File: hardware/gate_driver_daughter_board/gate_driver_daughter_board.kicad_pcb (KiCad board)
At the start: 2 copper layers, 103 x 116.3 mm, 66 parts, among them J1 Conn_01x08, J2 Conn_01x02, J3 Conn_01x02, U1 LF33_TO220, U2 REC20K-2412SZ, U3 6N137, U4 NCD57100DWR2G, U5 LTC6992CS6-2-TRMPBF, U6 LM7805_TO220, U7 MCP6004, U8 INA826, U9 LM7805_TO220

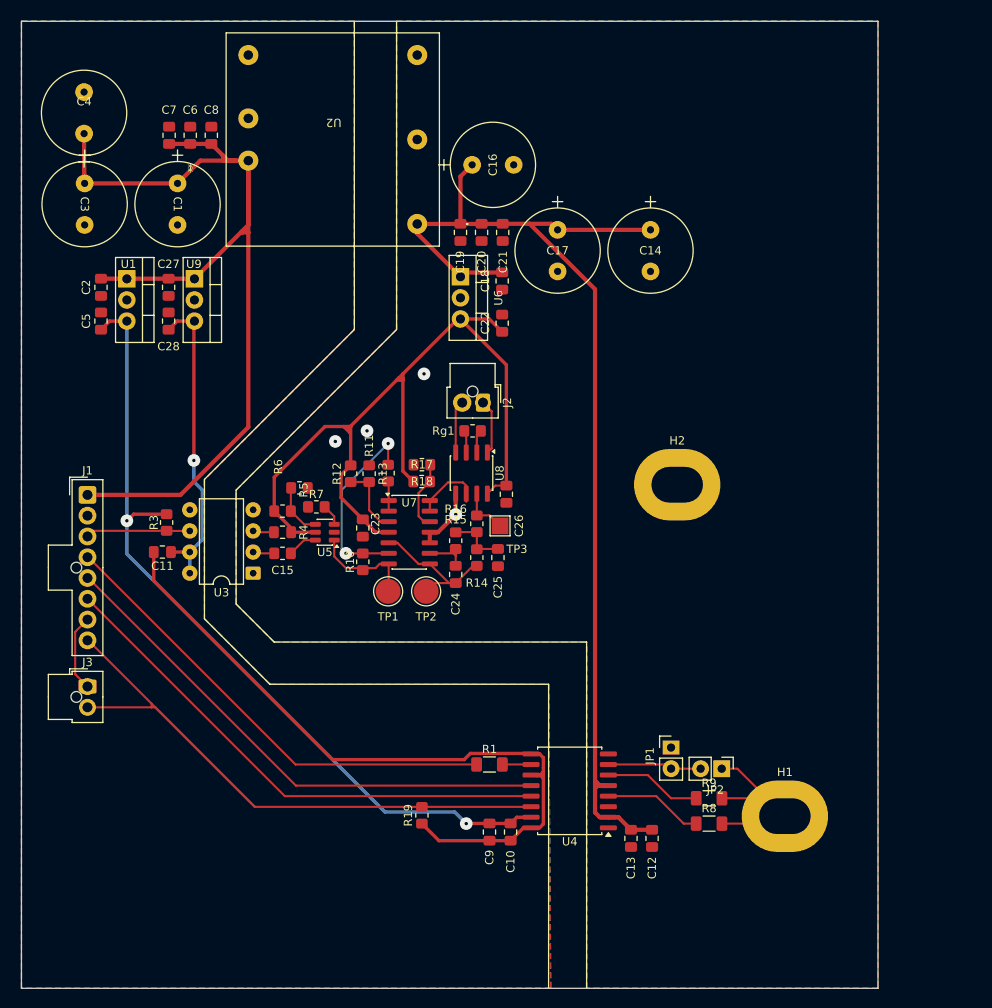
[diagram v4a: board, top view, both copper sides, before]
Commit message: V1.1, M60 Milling Accomodations
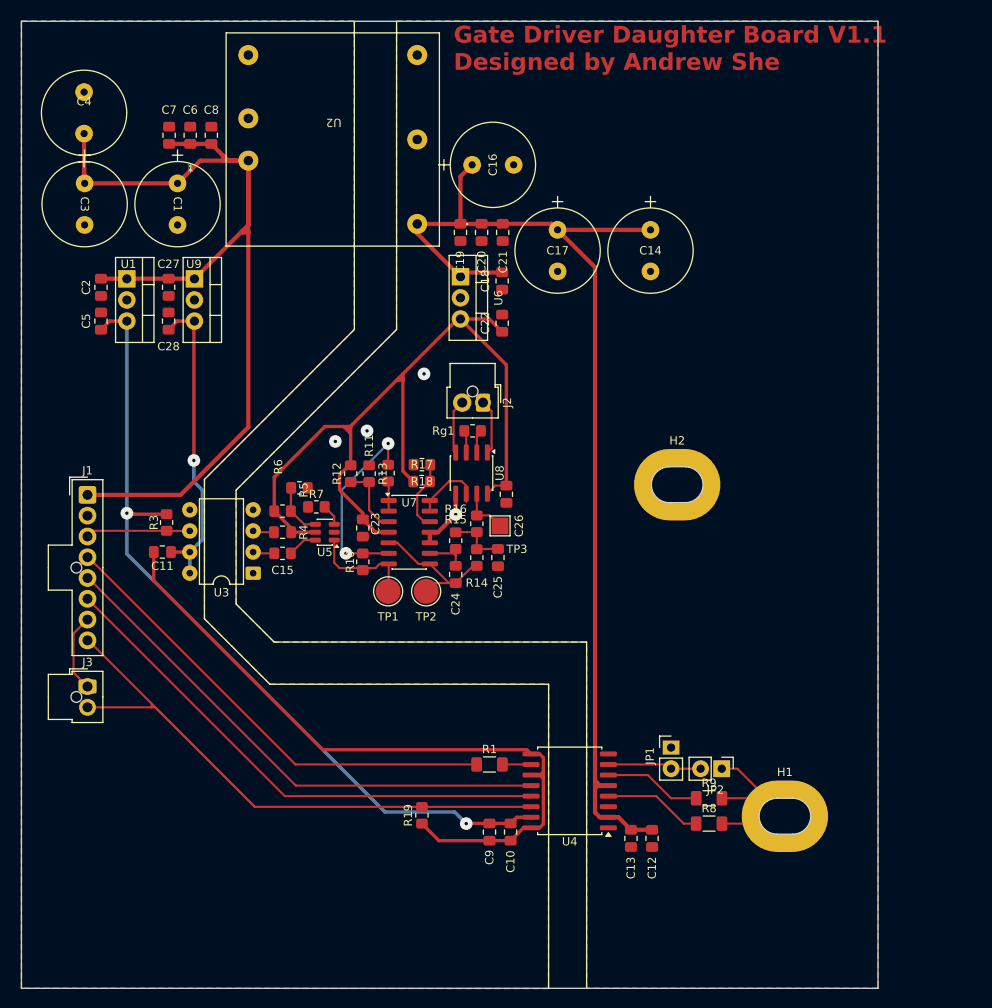
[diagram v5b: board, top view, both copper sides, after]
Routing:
- net +15V_Isolated: track 134.8 -> 133.7 mm
- net GND: track 87.4 -> 86.8 mm
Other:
- outline, holes or cut-outs redrawn
- board text added: "Gate Driver Daughter Board ${REVISION} Designed by Andrew She"

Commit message: V1.2, JLC Order PCB Updates
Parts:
- moved C16 1.05 mm to (151.6, 36.1)
- moved C6 0.07 mm to (117.3, 33.5)
- moved C7 0.07 mm to (114.8, 33.5)
- moved C8 0.07 mm to (119.9, 33.5)
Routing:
- net +15V_Isolated: track 133.7 -> 134.8 mm
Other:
- outline, holes or cut-outs redrawn
